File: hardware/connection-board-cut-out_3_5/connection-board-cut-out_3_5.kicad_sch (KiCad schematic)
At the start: 23 parts

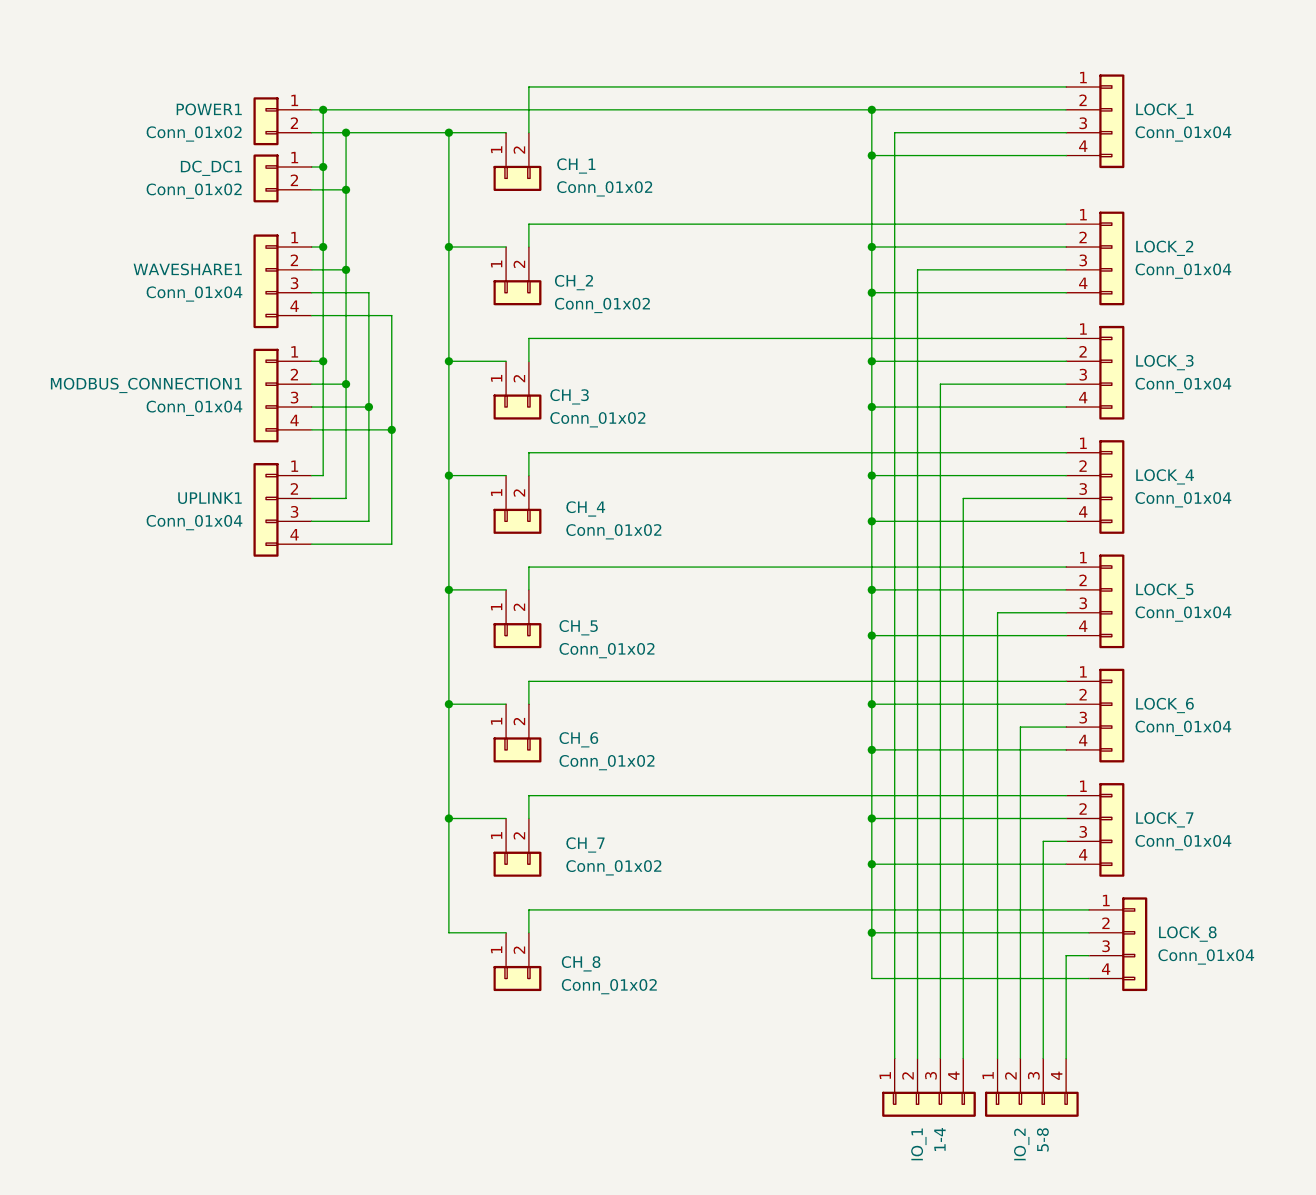
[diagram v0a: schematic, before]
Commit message: add 1N4007 diode between power supply and coil
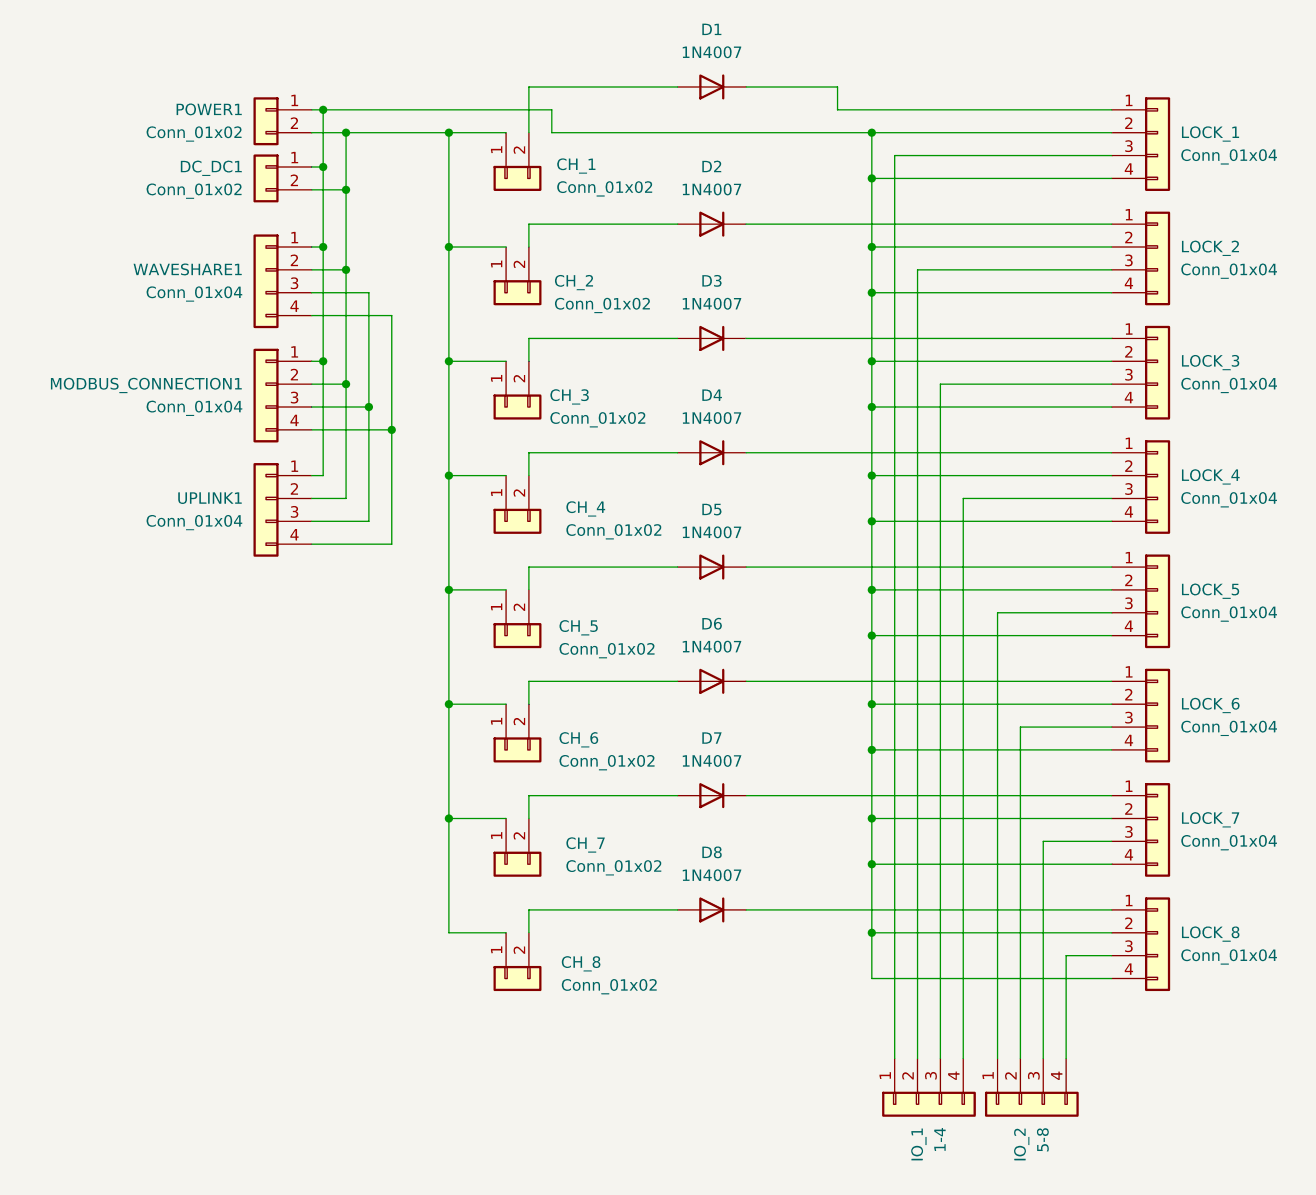
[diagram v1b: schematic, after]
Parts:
- added D1, D2, D3, D4, D5, D6, D7, D8: 1N4007, Diode_THT:D_DO-41_SOD81_P10.16mm_Horizontal, symbol Diode:1N4007
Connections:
- net at LOCK_4.1 (Pin_1): now also D4.1 (K); no longer CH_4.2 (Pin_2)
- net at LOCK_3.1 (Pin_1): now also D3.1 (K); no longer CH_3.2 (Pin_2)
- net at LOCK_2.1 (Pin_1): now also D2.1 (K); no longer CH_2.2 (Pin_2)
- net at LOCK_5.1 (Pin_1): now also D5.1 (K); no longer CH_5.2 (Pin_2)
- net at LOCK_8.1 (Pin_1): now also D8.1 (K); no longer CH_8.2 (Pin_2)
- net at CH_7.2 (Pin_2): now also D7.2 (A); no longer LOCK_7.1 (Pin_1)
- net at LOCK_1.1 (Pin_1): now also D1.1 (K); no longer CH_1.2 (Pin_2)
- net at LOCK_6.1 (Pin_1): now also D6.1 (K); no longer CH_6.2 (Pin_2)
- new net: CH_2.2 (Pin_2), D2.2 (A)
- new net: CH_1.2 (Pin_2), D1.2 (A)
- new net: CH_4.2 (Pin_2), D4.2 (A)
- new net: CH_6.2 (Pin_2), D6.2 (A)
- new net: CH_3.2 (Pin_2), D3.2 (A)
- new net: CH_5.2 (Pin_2), D5.2 (A)
- new net: D7.1 (K), LOCK_7.1 (Pin_1)
- new net: CH_8.2 (Pin_2), D8.2 (A)
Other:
- moved on the sheet: LOCK_1, LOCK_2, LOCK_3, LOCK_4, LOCK_5, LOCK_6, LOCK_7, LOCK_8
